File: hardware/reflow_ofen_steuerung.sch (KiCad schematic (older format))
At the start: 41 parts, among them J1 230VAC, J10 GND, J2 Heizung oben, J3 Heizung unten, J4 AVR-ISP-6, J5 LCD Display, J6 Encoder, J7 FAN, J8 +5V, J9 +12V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

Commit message: PCB angepasst für Kühlkörper der Spannungsregler
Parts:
- D2: footprint LED_THT:LED_D3.0mm -> LED_THT:LED_D5.0mm
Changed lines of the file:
@@
 F 0 "D2" H 9943 3145 50  0000 C CNN
 F 1 "LED" H 9943 3236 50  0000 C CNN
-F 2 "LED_THT:LED_D3.0mm" H 9950 3400 50  0001 C CNN
+F 2 "LED_THT:LED_D5.0mm" H 9950 3400 50  0001 C CNN
 F 3 "~" H 9950 3400 50  0001 C CNN
 	1    9950 3400

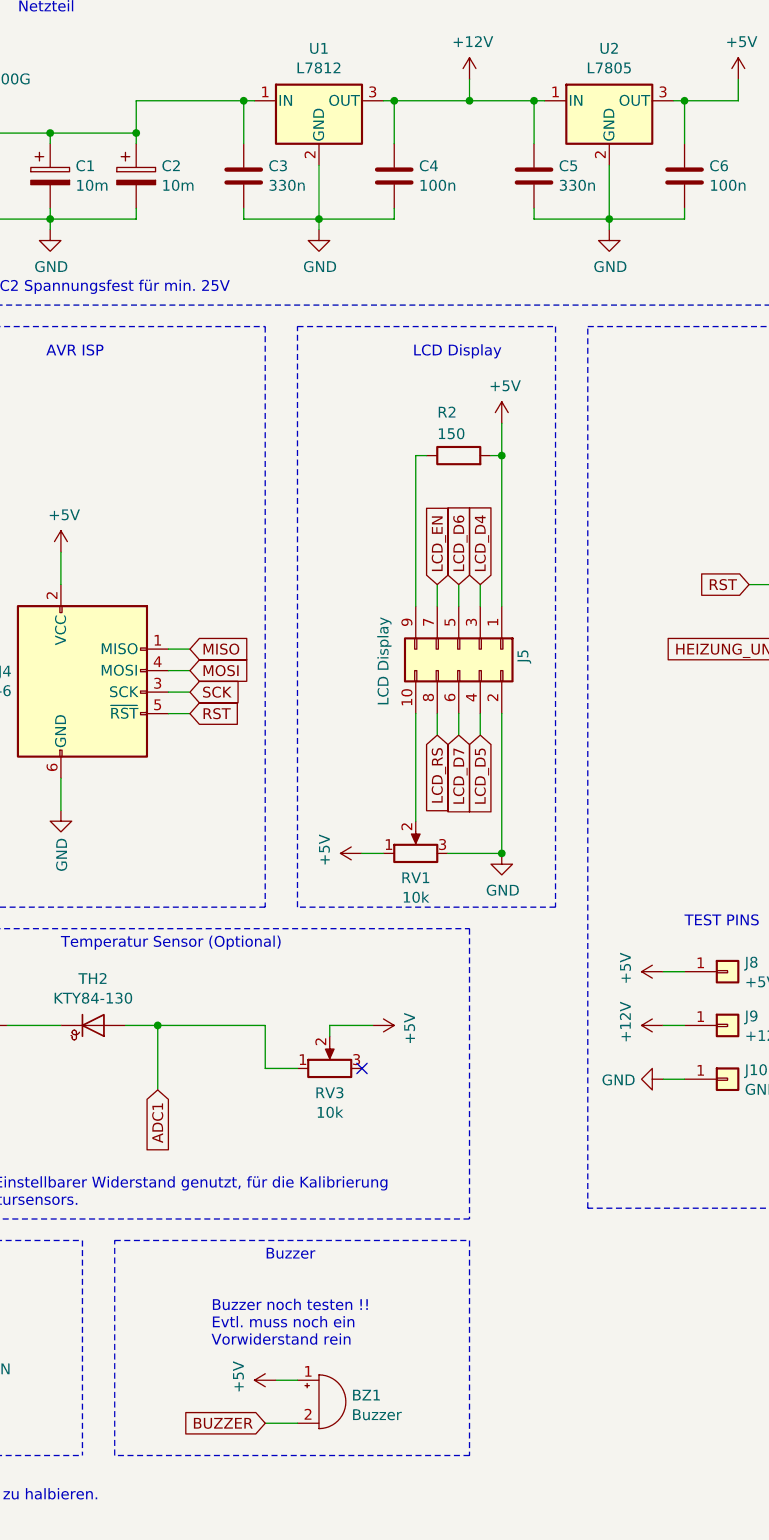
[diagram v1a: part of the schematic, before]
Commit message: added 150 ohm resistor for buzzer
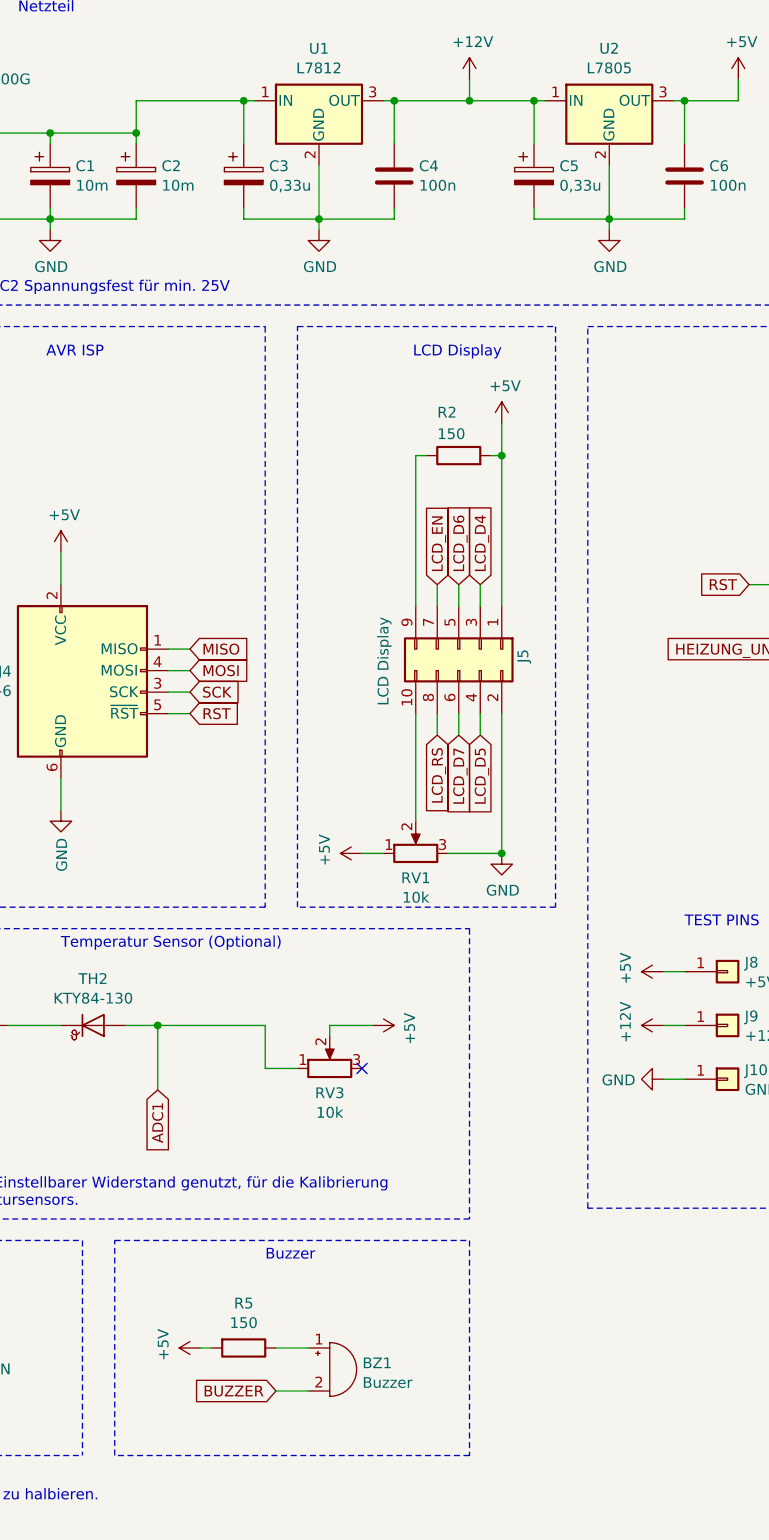
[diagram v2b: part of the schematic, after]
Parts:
- removed C3, C5: 330n, Capacitor_THT:C_Disc_D5.0mm_W2.5mm_P2.50mm, symbol Device:C
- added C3, C5: 0,33u, Capacitor_THT:CP_Radial_D4.0mm_P1.50mm, symbol Device:CP
- added R5: 150, Resistor_THT:R_Axial_DIN0207_L6.3mm_D2.5mm_P7.62mm_Horizontal, symbol Device:R
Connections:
- net +12V: now also C5.1
- net +5V: now also R5.2; no longer BZ1.1 (-)
- net GND: now also C3.2, C5.2
- net at C1.1, C2.1, D1.1 (+)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: now also C3.1
- new net: BZ1.1 (-), R5.1
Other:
- note removed: "Buzzer noch testen !!\nEvtl. muss noch ein \nVorwiderstand rein\n"
- moved on the sheet: BZ1
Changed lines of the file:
@@
 Sheet 1 1
 Title "Steuerung für Umbau Pizzaofen zu Reflow Ofen"
-Date "2020-10-02"
+Date "2020-10-22"
 Rev "V1.0.0"
 Comp "Thorsten Kattanek"
@@
 	5750 1150 5800 1150
 $Comp
-L Device:C C3
-U 1 1 5F6F3D36
-P 5100 1500
-F 0 "C3" H 5215 1546 50  0000 L CNN
-F 1 "330n" H 5215 1455 50  0000 L CNN
-F 2 "Capacitor_THT:C_Disc_D5.0mm_W2.5mm_P2.50mm" H 5138 1350 50  0001 C CNN
-F 3 "~" H 5100 1500 50  0001 C CNN
-	1    5100 1500
-	1    0    0    -1
-$EndComp
-$Comp
 L Device:C C4
 U 1 1 5F6F69E0
@@
 Wire Wire Line
 	7100 1150 7150 1150
-$Comp
-L Device:C C5
-U 1 1 5F70263D
-P 6450 1500
-F 0 "C5" H 6565 1546 50  0000 L CNN
-F 1 "330n" H 6565 1455 50  0000 L CNN
-F 2 "Capacitor_THT:C_Disc_D5.0mm_W2.5mm_P2.50mm" H 6488 1350 50  0001 C CNN
-F 3 "~" H 6450 1500 50  0001 C CNN
-	1    6450 1500
-	1    0    0    -1
-$EndComp
 $Comp
 L Device:C C6
@@
 L Device:Buzzer BZ1
 U 1 1 5F929A25
-P 5450 7200
-F 0 "BZ1" H 5602 7229 50  0000 L CNN
-F 1 "Buzzer" H 5602 7138 50  0000 L CNN
-F 2 "Buzzer_Beeper:Buzzer_TDK_PS1240P02BT_D12.2mm_H6.5mm" V 5425 7300 50  0001 C CNN
-F 3 "~" V 5425 7300 50  0001 C CNN
-	1    5450 7200
+P 5500 7050
+F 0 "BZ1" H 5652 7079 50  0000 L CNN
+F 1 "Buzzer" H 5652 6988 50  0000 L CNN
+F 2 "Buzzer_Beeper:Buzzer_TDK_PS1240P02BT_D12.2mm_H6.5mm" V 5475 7150 50  0001 C CNN
+F 3 "~" V 5475 7150 50  0001 C CNN
+	1    5500 7050
 	1    0    0    -1
 $EndComp
@@
 L power:+5V #PWR018
 U 1 1 5F9368A1
-P 5250 7100
-F 0 "#PWR018" H 5250 6950 50  0001 C CNN
-F 1 "+5V" H 5265 7273 50  0000 C CNN
-F 2 "" H 5250 7100 50  0001 C CNN
-F 3 "" H 5250 7100 50  0001 C CNN
-	1    5250 7100
+P 4900 6950
+F 0 "#PWR018" H 4900 6800 50  0001 C CNN
+F 1 "+5V" H 4915 7123 50  0000 C CNN
+F 2 "" H 4900 6950 50  0001 C CNN
+F 3 "" H 4900 6950 50  0001 C CNN
+	1    4900 6950
 	0    -1   -1   0
 $EndComp
 Wire Wire Line
-	5250 7100 5350 7100
-Text Notes 4950 6950 0    50   ~ 0
-Buzzer noch testen !!\nEvtl. muss noch ein \nVorwiderstand rein\n
+	5250 6950 5400 6950
 Wire Notes Line
 	4500 6450 6150 6450
@@
 Wire Wire Line
 	9300 4600 9450 4600
-Text GLabel 5200 7300 0    50   Input ~ 0
+Text GLabel 5250 7150 0    50   Input ~ 0
 BUZZER
 Wire Wire Line
-	5200 7300 5350 7300
+	5250 7150 5400 7150
 Text Notes 5200 6550 0    50   ~ 0
 Buzzer
@@
 EndData
 $EndBitmap
+$Comp
+L Device:CP C3
+U 1 1 5F87F0C5
+P 5100 1500
+F 0 "C3" H 5218 1546 50  0000 L CNN
+F 1 "0,33u" H 5218 1455 50  0000 L CNN
+F 2 "Capacitor_THT:CP_Radial_D4.0mm_P1.50mm" H 5138 1350 50  0001 C CNN
+F 3 "~" H 5100 1500 50  0001 C CNN
+	1    5100 1500
+	1    0    0    -1
+$EndComp
+$Comp
+L Device:CP C5
+U 1 1 5F89C4E3
+P 6450 1500
+F 0 "C5" H 6568 1546 50  0000 L CNN
+F 1 "0,33u" H 6568 1455 50  0000 L CNN
+F 2 "Capacitor_THT:CP_Radial_D4.0mm_P1.50mm" H 6488 1350 50  0001 C CNN
+F 3 "~" H 6450 1500 50  0001 C CNN
+	1    6450 1500
+	1    0    0    -1
+$EndComp
+$Comp
+L Device:R R5
+U 1 1 5F927DB6
+P 5100 6950
+F 0 "R5" V 4893 6950 50  0000 C CNN
+F 1 "150" V 4984 6950 50  0000 C CNN
+F 2 "Resistor_THT:R_Axial_DIN0207_L6.3mm_D2.5mm_P7.62mm_Horizontal" V 5030 6950 50  0001 C CNN
+F 3 "~" H 5100 6950 50  0001 C CNN
+	1    5100 6950
+	0    1    1    0
+$EndComp
+Wire Wire Line
+	4900 6950 4950 6950
 $EndSCHEMATC

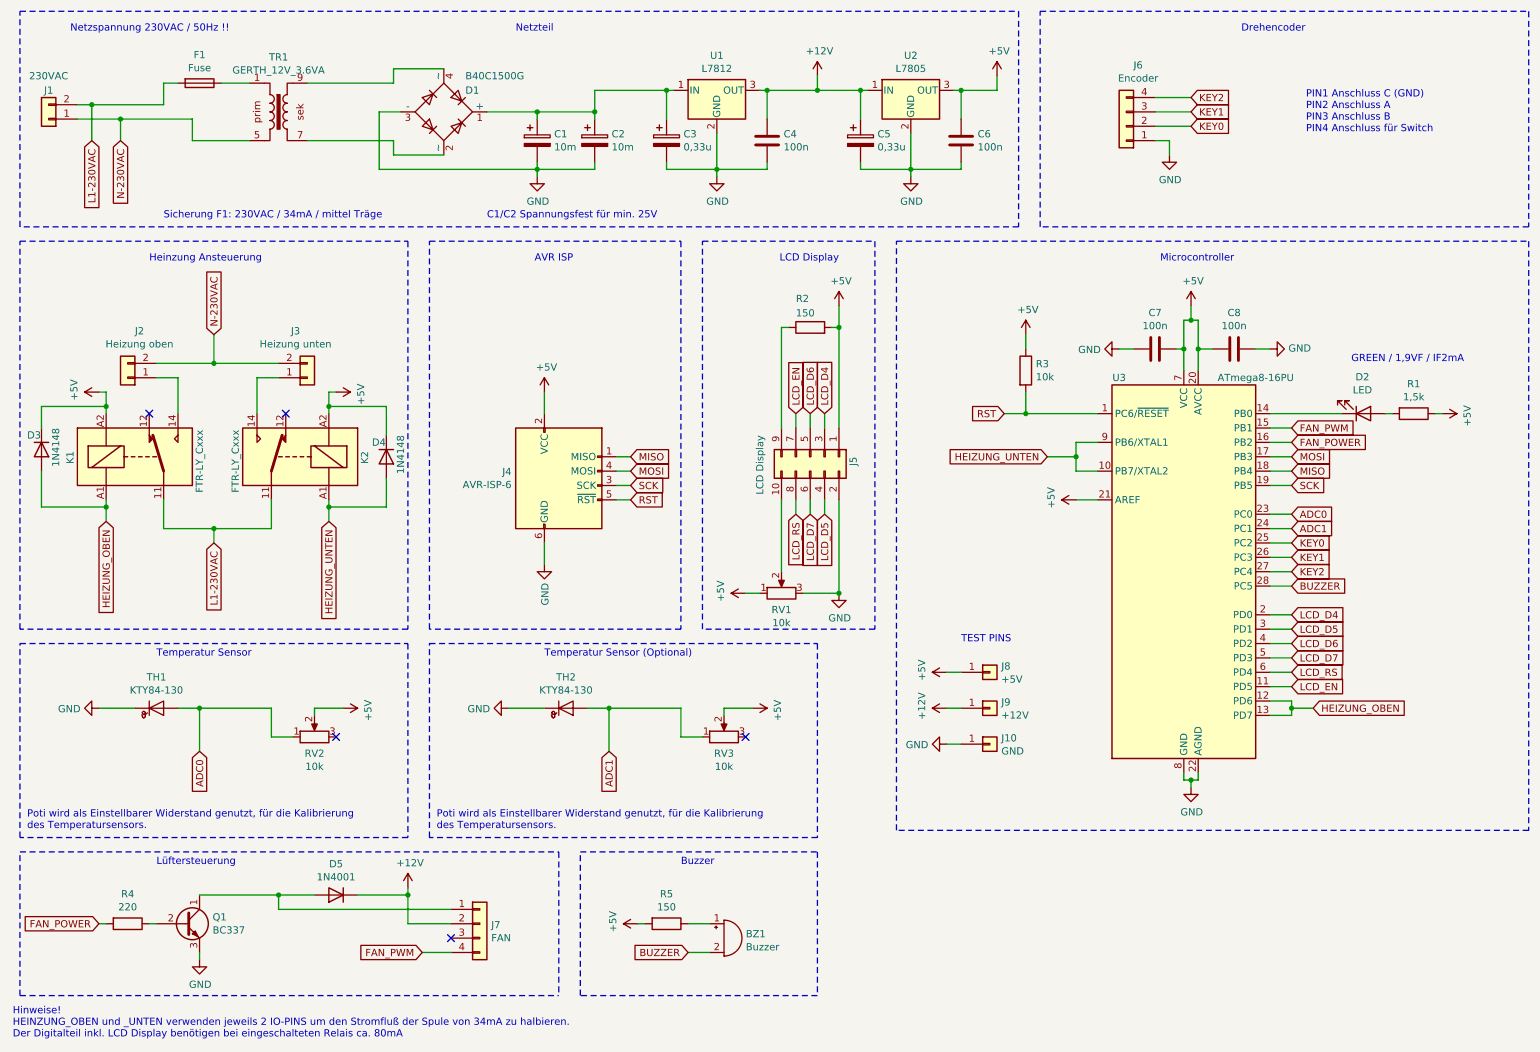
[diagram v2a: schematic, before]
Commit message: changed label ADC0/1 to TEMP_SENSOR1/2
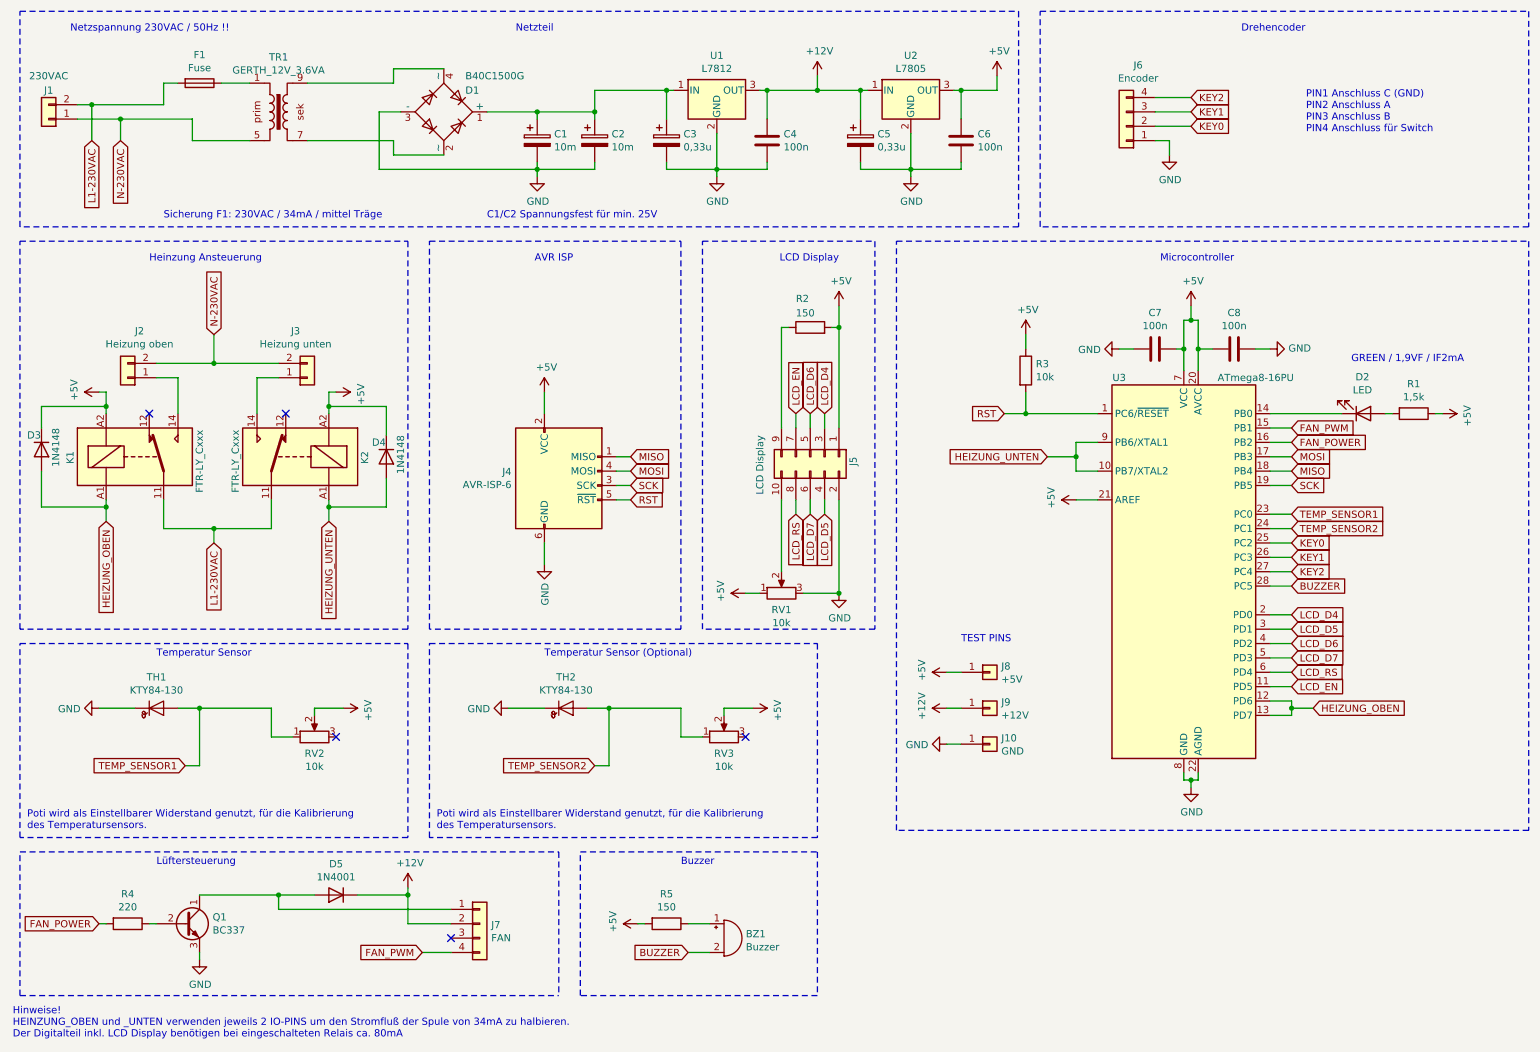
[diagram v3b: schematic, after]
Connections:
- net ADC0 renamed TEMP_SENSOR1
- net ADC1 renamed TEMP_SENSOR2
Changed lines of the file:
@@
 Sheet 1 1
 Title "Steuerung für Umbau Pizzaofen zu Reflow Ofen"
-Date "2020-10-22"
+Date "2020-10-24"
 Rev "V1.0.0"
 Comp "Thorsten Kattanek"
@@
 	2650 5450 2850 5450
 Text GLabel 9450 4100 2    50   Input ~ 0
-ADC0
-Text GLabel 1850 5750 3    50   Input ~ 0
-ADC0
-Wire Wire Line
-	1850 5750 1850 5450
+TEMP_SENSOR1
+Text GLabel 1750 5850 0    50   Input ~ 0
+TEMP_SENSOR1
 Wire Notes Line
 	600  5000 3300 5000
@@
 Wire Wire Line
 	5500 5450 5700 5450
-Text GLabel 4700 5750 3    50   Input ~ 0
-ADC1
-Wire Wire Line
-	4700 5750 4700 5450
+Text GLabel 4600 5850 0    50   Input ~ 0
+TEMP_SENSOR2
 Wire Notes Line
 	3450 5000 6150 5000
@@
 Poti wird als Einstellbarer Widerstand genutzt, für die Kalibrierung\ndes Temperatursensors.
 Text GLabel 9450 4200 2    50   Input ~ 0
-ADC1
+TEMP_SENSOR2
 Wire Wire Line
 	9300 4200 9450 4200
@@
 Wire Wire Line
 	4900 6950 4950 6950
+Wire Wire Line
+	4600 5850 4700 5850
+Wire Wire Line
+	4700 5450 4700 5850
+Wire Wire Line
+	1750 5850 1850 5850
+Wire Wire Line
+	1850 5450 1850 5850
 $EndSCHEMATC

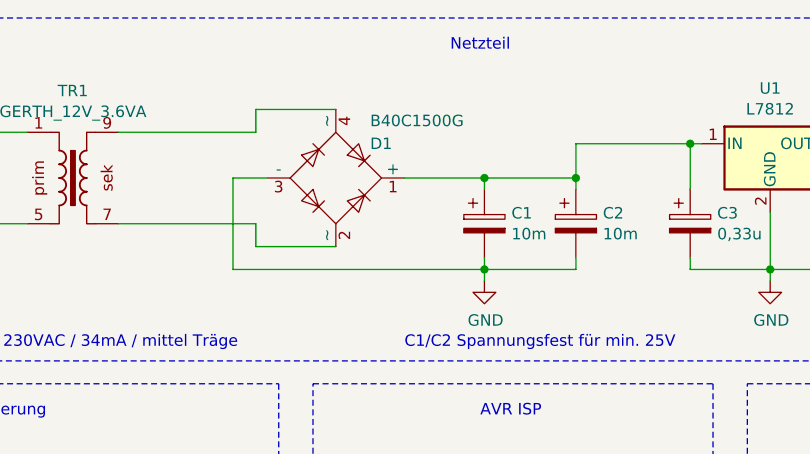
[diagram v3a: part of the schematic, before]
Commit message: Brückengleichrichter D1 korrigiert
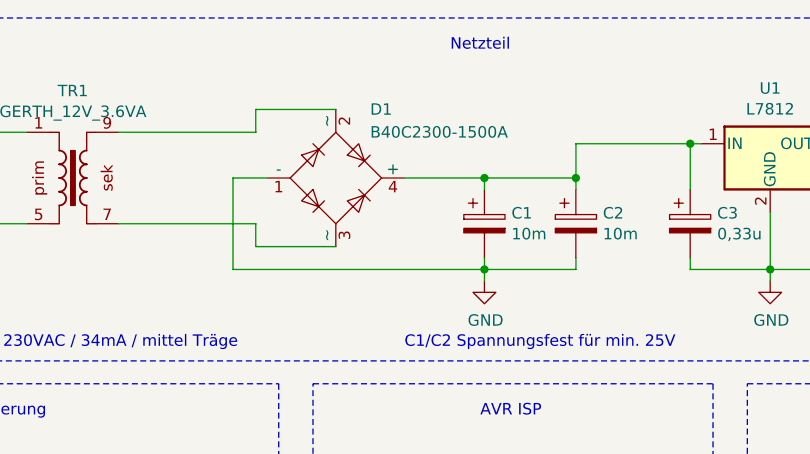
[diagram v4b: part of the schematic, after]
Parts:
- removed D1: B40C1500G, Diode_THT:Diode_Bridge_Vishay_GBL, symbol Diode_Bridge:B40C1500G
- added D1: B40C2300-1500A, Diode_THT:Diode_Bridge_19.0x3.5x10.0mm_P5.0mm, symbol Diode_Bridge:B40C2300-1500A
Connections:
- net GND: now also D1.1 (-)
- net at C1.1, C2.1, C3.1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: now also D1.4 (+)
- net at TR1.7: now also D1.3 (~~)
- net at TR1.9: now also D1.2 (~~)
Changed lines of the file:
@@
 Sheet 1 1
 Title "Steuerung für Umbau Pizzaofen zu Reflow Ofen"
-Date "2020-10-24"
-Rev "V1.0.0"
+Date "2020-11-20"
+Rev "V1.0.1"
 Comp "Thorsten Kattanek"
 Comment1 ""
@@
 	4600 1700 4600 1650
 Connection ~ 4200 1700
-$Comp
-L Diode_Bridge:B40C1500G D1
-U 1 1 5F66BA49
-P 3550 1300
-F 0 "D1" H 3700 1450 50  0000 L CNN
-F 1 "B40C1500G" H 3700 1550 50  0000 L CNN
-F 2 "Diode_THT:Diode_Bridge_Vishay_GBL" H 3700 1425 50  0001 L CNN
-F 3 "https://www.vishay.com/docs/88501/b40c1500g.pdf" H 3550 1300 50  0001 C CNN
-	1    3550 1300
-	1    0    0    -1
-$EndComp
 $Comp
 L transformer_tk:GERTH_12V_3.6VA TR1
@@
 Wire Wire Line
 	1850 5450 1850 5850
+$Comp
+L Diode_Bridge:B40C2300-1500A D1
+U 1 1 5FB8F7B1
+P 3550 1300
+F 0 "D1" H 3700 1600 50  0000 L CNN
+F 1 "B40C2300-1500A" H 3700 1500 50  0000 L CNN
+F 2 "Diode_THT:Diode_Bridge_19.0x3.5x10.0mm_P5.0mm" H 3700 1425 50  0001 L CNN
+F 3 "https://diotec.com/tl_files/diotec/files/pdf/datasheets/b40c2300.pdf" H 3550 1300 50  0001 C CNN
+	1    3550 1300
+	1    0    0    -1
+$EndComp
 $EndSCHEMATC
